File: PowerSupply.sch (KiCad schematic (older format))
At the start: 3 parts, among them U2 MCP1700T-3302E-TT

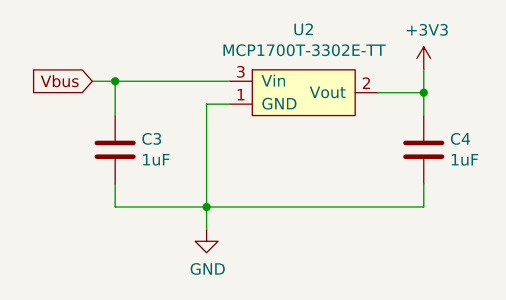
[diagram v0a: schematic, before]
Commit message: Initial layout complete. Pins moved to make layout easy
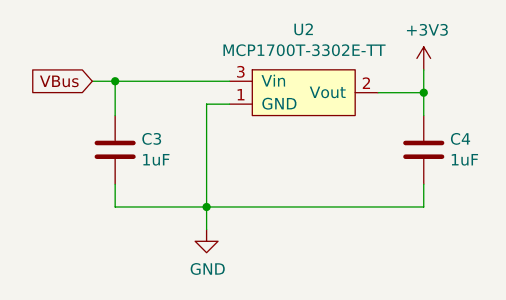
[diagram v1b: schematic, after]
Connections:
- net Vbus renamed VBus
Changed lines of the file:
@@
 $EndDescr
 Text GLabel 5300 3550 0    50   Input ~ 0
-Vbus
+VBus
 $Comp
 L power:GND #PWR09
